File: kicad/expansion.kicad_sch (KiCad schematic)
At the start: 8 parts, among them J10 Slot 2, J11 Slot 3, J12 Slot 4, J9 Slot 1

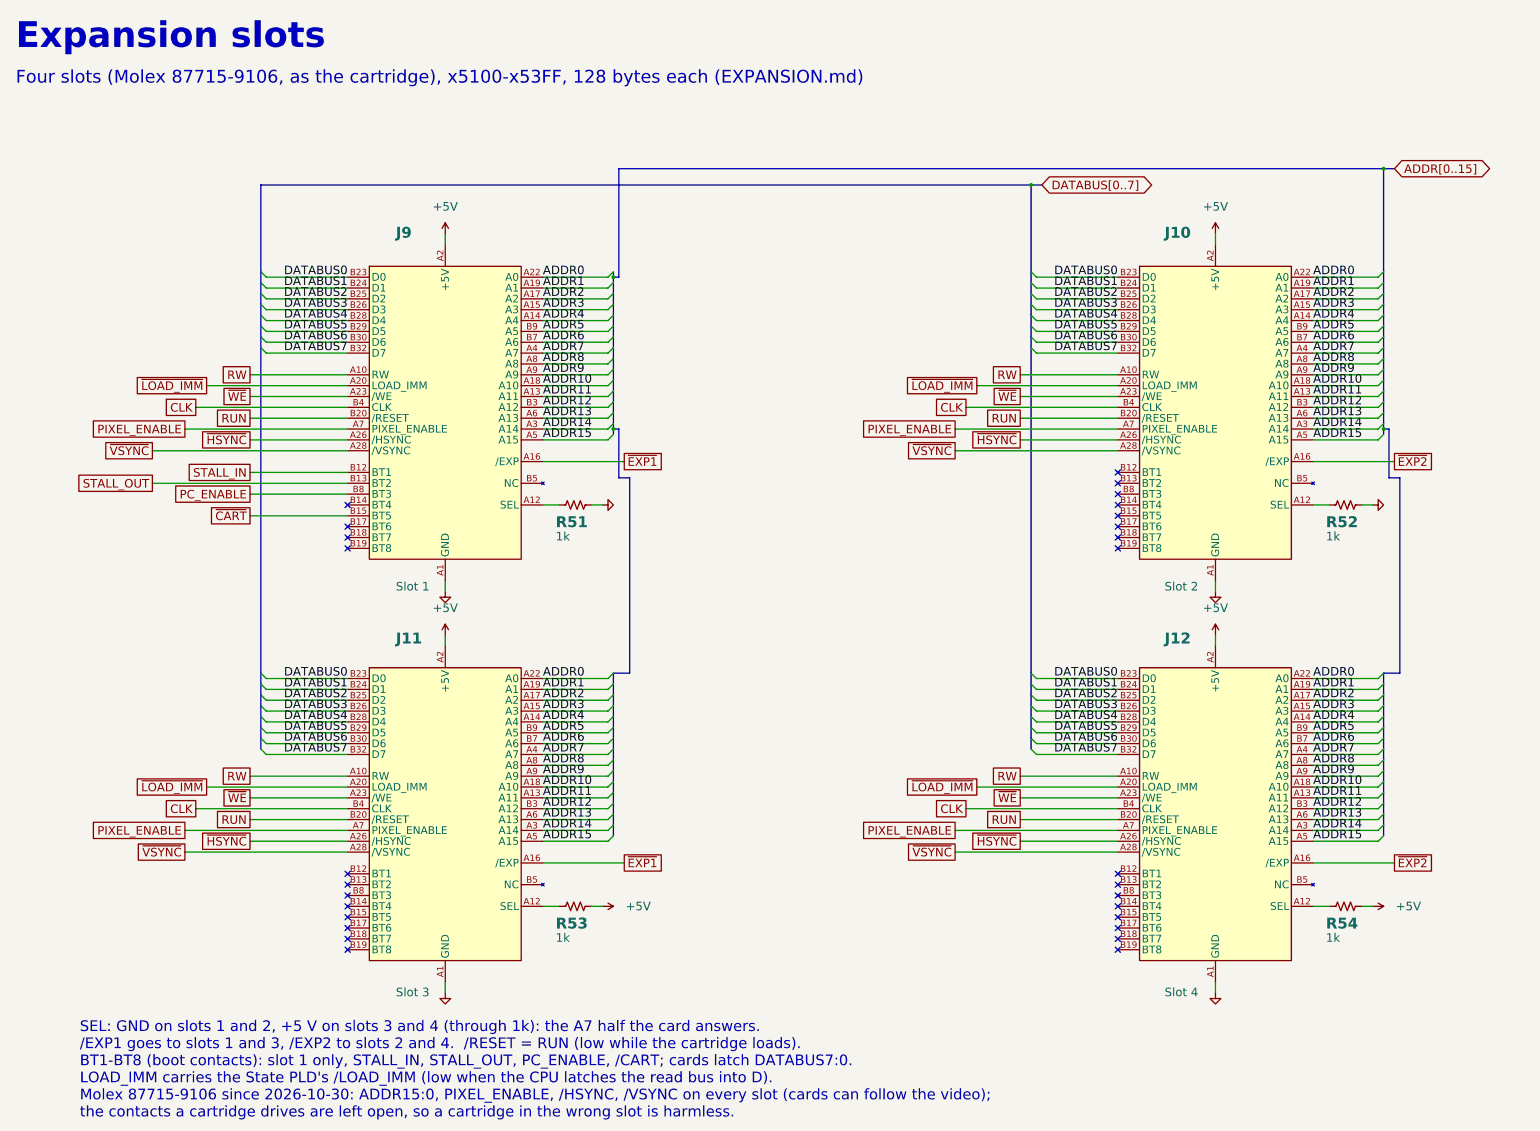
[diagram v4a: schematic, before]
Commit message: Expansion slots: grounds on the inner rows, signals outer; take in Justin's KiCad edits
Reassign the expansion slot contacts so the extra grounds sit on the
inner (even) rows and the signals on the outer (odd) rows wherever the
cartridge pinout allows: 19 of 38 signals outer.  The cartridge's power
and ground contacts, the shared signals and the wrong-slot rules are
kept (every expansion output and extra ground on a J8 spare, every
cartridge output open on the expansion slot).  BT4 and BT6-BT8 dropped.

Justin's local KiCad edits (all main-board sheets, the board and the
project; K1 coil pins swapped) are committed as he saved them; only the
expansion sheet comes from the generator.  Netlist differs from his
only on J9-J12; ERC unchanged.

Co-Authored-By: Claude Opus 5.5 <noreply@anthropic.com>
Claude-Session: https://claude.ai/code/session_01DnW5SUDtmC2C2nXUS4xVk2
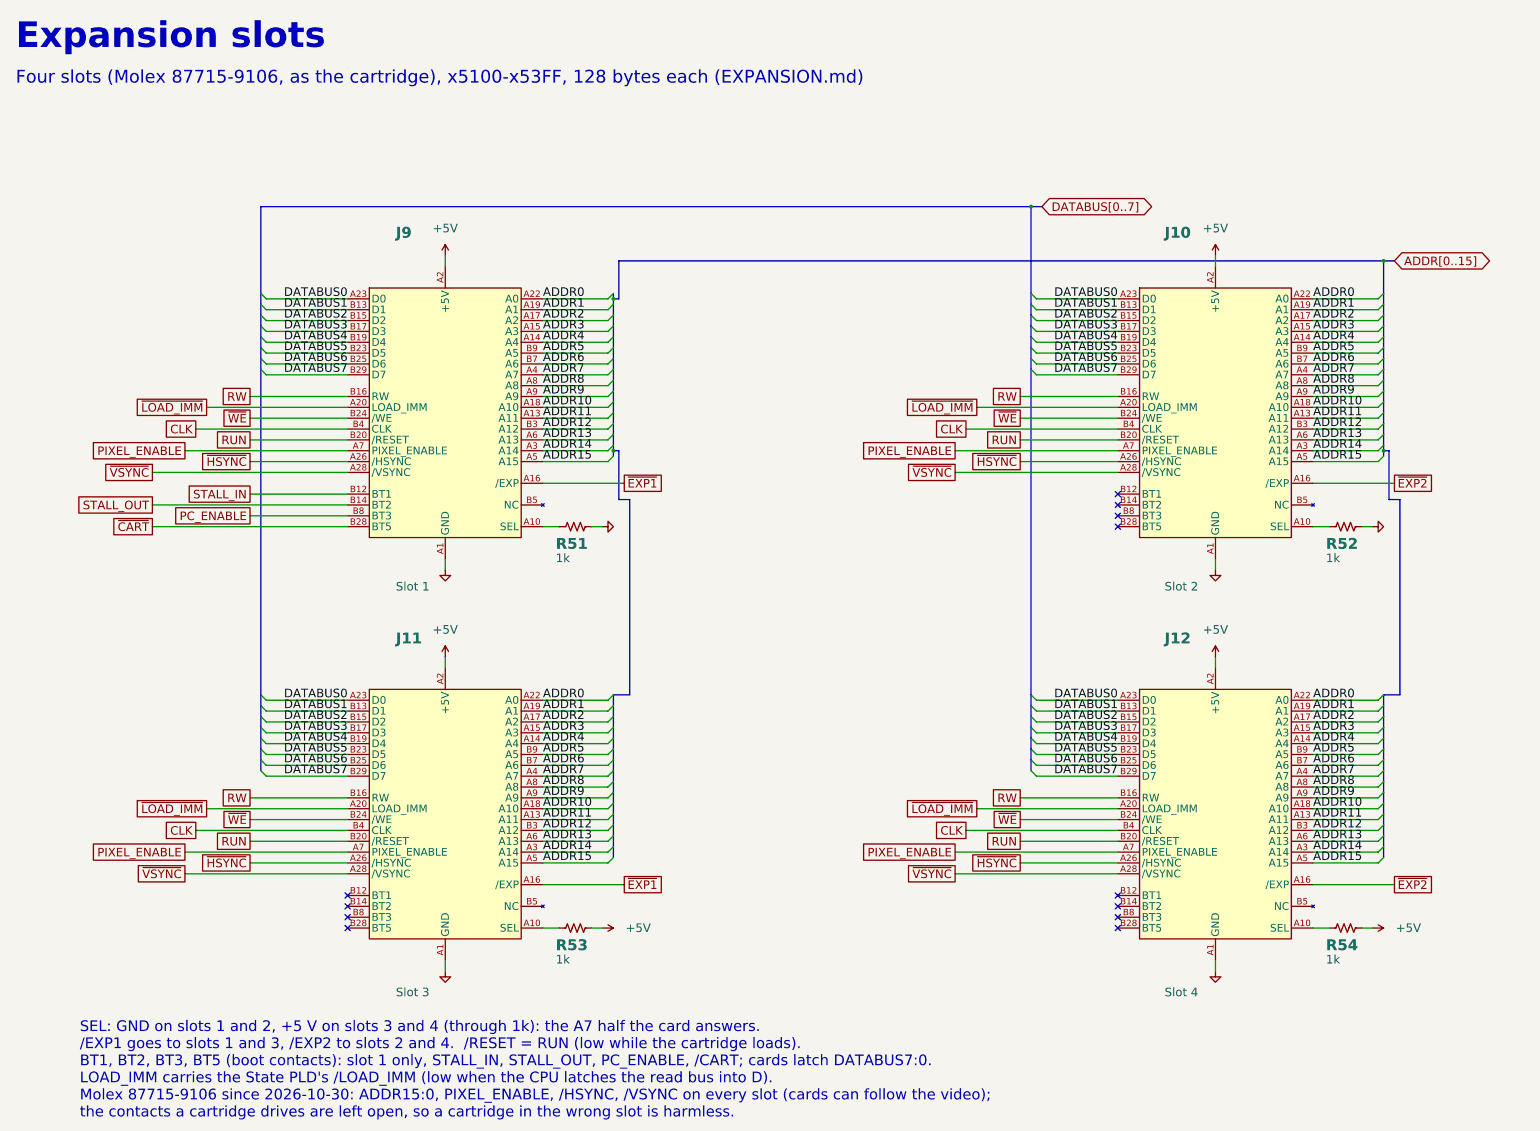
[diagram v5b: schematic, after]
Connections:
- net DATABUS0: now also J10.A23 (D0), J11.A23 (D0), J12.A23 (D0), J9.A23 (D0); no longer J10.B23 (D0), J11.B23 (D0), J12.B23 (D0), J9.B23 (D0)
- net DATABUS1: now also J10.B13 (D1), J11.B13 (D1), J12.B13 (D1), J9.B13 (D1); no longer J10.B24 (D1), J11.B24 (D1), J12.B24 (D1), J9.B24 (D1)
- net DATABUS2: now also J10.B15 (D2), J11.B15 (D2), J12.B15 (D2), J9.B15 (D2); no longer J10.B25 (D2), J11.B25 (D2), J12.B25 (D2), J9.B25 (D2)
- net DATABUS3: now also J10.B17 (D3), J11.B17 (D3), J12.B17 (D3), J9.B17 (D3); no longer J10.B26 (D3), J11.B26 (D3), J12.B26 (D3), J9.B26 (D3)
- net DATABUS4: now also J10.B19 (D4), J11.B19 (D4), J12.B19 (D4), J9.B19 (D4); no longer J10.B28 (D4), J11.B28 (D4), J12.B28 (D4), J9.B28 (D4)
- net DATABUS5: now also J10.B23 (D5), J11.B23 (D5), J12.B23 (D5), J9.B23 (D5); no longer J10.B29 (D5), J11.B29 (D5), J12.B29 (D5), J9.B29 (D5)
- net DATABUS6: now also J10.B25 (D6), J11.B25 (D6), J12.B25 (D6), J9.B25 (D6); no longer J10.B30 (D6), J11.B30 (D6), J12.B30 (D6), J9.B30 (D6)
- net DATABUS7: now also J10.B29 (D7), J11.B29 (D7), J12.B29 (D7), J9.B29 (D7); no longer J10.B32 (D7), J11.B32 (D7), J12.B32 (D7), J9.B32 (D7)
- net GND: now also J10.A12 (GND), J10.B18 (GND), J10.B26 (GND), J10.B30 (GND), J10.B32 (GND), J11.A12 (GND), J11.B18 (GND), J11.B26 (GND), J11.B30 (GND), J11.B32 (GND), J12.A12 (GND), J12.B18 (GND), J12.B26 (GND), J12.B30 (GND), J12.B32 (GND), J9.A12 (GND), J9.B18 (GND), J9.B26 (GND), J9.B30 (GND), J9.B32 (GND)
- net RW: now also J10.B16 (RW), J11.B16 (RW), J12.B16 (RW), J9.B16 (RW); no longer J10.A10 (RW), J11.A10 (RW), J12.A10 (RW), J9.A10 (RW)
- net STALL_OUT: now also J9.B14 (BT2); no longer J9.B13 (BT2)
- net ~{CART}: now also J9.B28 (BT5); no longer J9.B15 (BT5)
- net ~{WE}: now also J10.B24 (/WE), J11.B24 (/WE), J12.B24 (/WE), J9.B24 (/WE); no longer J10.A23 (/WE), J11.A23 (/WE), J12.A23 (/WE), J9.A23 (/WE)
- net at R53.1: now also J11.A10 (SEL); no longer J11.A12 (SEL)
- net at J11.A24 (NC), J11.A25 (NC), J11.A27 (NC)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: no longer J11.B16 (NC)
- net at R54.1: now also J12.A10 (SEL); no longer J12.A12 (SEL)
- net at J12.A24 (NC), J12.A25 (NC), J12.A27 (NC)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: no longer J12.B16 (NC)
- net at R51.1: now also J9.A10 (SEL); no longer J9.A12 (SEL)
- net at R52.1: now also J10.A10 (SEL); no longer J10.A12 (SEL)
- net at J10.A24 (NC), J10.A25 (NC), J10.A27 (NC)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: no longer J10.B16 (NC)
- net at J9.A24 (NC), J9.A25 (NC), J9.A27 (NC)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: no longer J9.B16 (NC)
- no-connect marks 28 -> 12
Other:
- note added: "BT1, BT2, BT3, BT5 (boot contacts): slot 1 only, STALL_IN, STALL_OUT, PC_ENABLE, /CART; cards latch DATABUS7:0."
- note removed: "BT1-BT8 (boot contacts): slot 1 only, STALL_IN, STALL_OUT, PC_ENABLE, /CART; cards latch DATABUS7:0."
- moved on the sheet: R51, R52, R53, R54

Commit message: Expansion slots: slot 1 nearest the board center
Swap the symbol uuids of J9/J12, J10/J11, R51/R54 and R52/R53 in the
expansion sheet, so Update PCB from Schematic renames the footprints in
place: slot 1 (J9, boot contacts, /EXP1, SEL GND) lands on the slot at
x 175, nearest the center, and slot 4 on the outermost one at x 94.  No
footprint moves.  Justin's latest board (routing since PR #196) is
committed as he saved it.

Co-Authored-By: Claude Opus 5.5 <noreply@anthropic.com>
Claude-Session: https://claude.ai/code/session_01DnW5SUDtmC2C2nXUS4xVk2
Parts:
- J10: renamed from J11; value Slot 3 -> Slot 2
- J11: renamed from J10; value Slot 2 -> Slot 3
- J12: renamed from J9; value Slot 1 -> Slot 4
- J9: renamed from J12; value Slot 4 -> Slot 1
- renumbered R54 to R51, R53 to R52, R52 to R53, R51 to R54
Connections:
- net +5V: now also R53.2, R54.2; no longer R51.2, R52.2
- net GND: now also R51.2, R52.2; no longer R53.2, R54.2
- net PC_ENABLE: now also J9.B8 (BT3); no longer J12.B8 (BT3)
- net STALL_IN: now also J9.B12 (BT1); no longer J12.B12 (BT1)
- net STALL_OUT: now also J9.B14 (BT2); no longer J12.B14 (BT2)
- net ~{CART}: now also J9.B28 (BT5); no longer J12.B28 (BT5)
- net ~{EXP1}: now also J11.A16 (/EXP), J9.A16 (/EXP); no longer J10.A16 (/EXP), J12.A16 (/EXP)
- net ~{EXP2}: now also J10.A16 (/EXP), J12.A16 (/EXP); no longer J11.A16 (/EXP), J9.A16 (/EXP)
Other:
- moved on the sheet: J10, J11, J12, J9, R51, R52, R53, R54
